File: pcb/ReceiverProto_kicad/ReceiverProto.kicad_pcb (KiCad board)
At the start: 4 copper layers, 75 x 50 mm, 65 parts, among them J1 Conn_01x09, J2 Conn_01x03, J3 Conn_01x04, J4 Conn_01x06, U11 ADM8660ARZ-REEL, U12 ADP7182AUJZ-1.8-R7, U13 ADA4807-1, U14 ADA4807-1, U15 ADA4807-1, U16 ADA4807-1, U4 AD7387BCPZ-RL7, U5 TLV9001IDCK, U6 TLV9001IDCK, U7 TPS79301DBVR

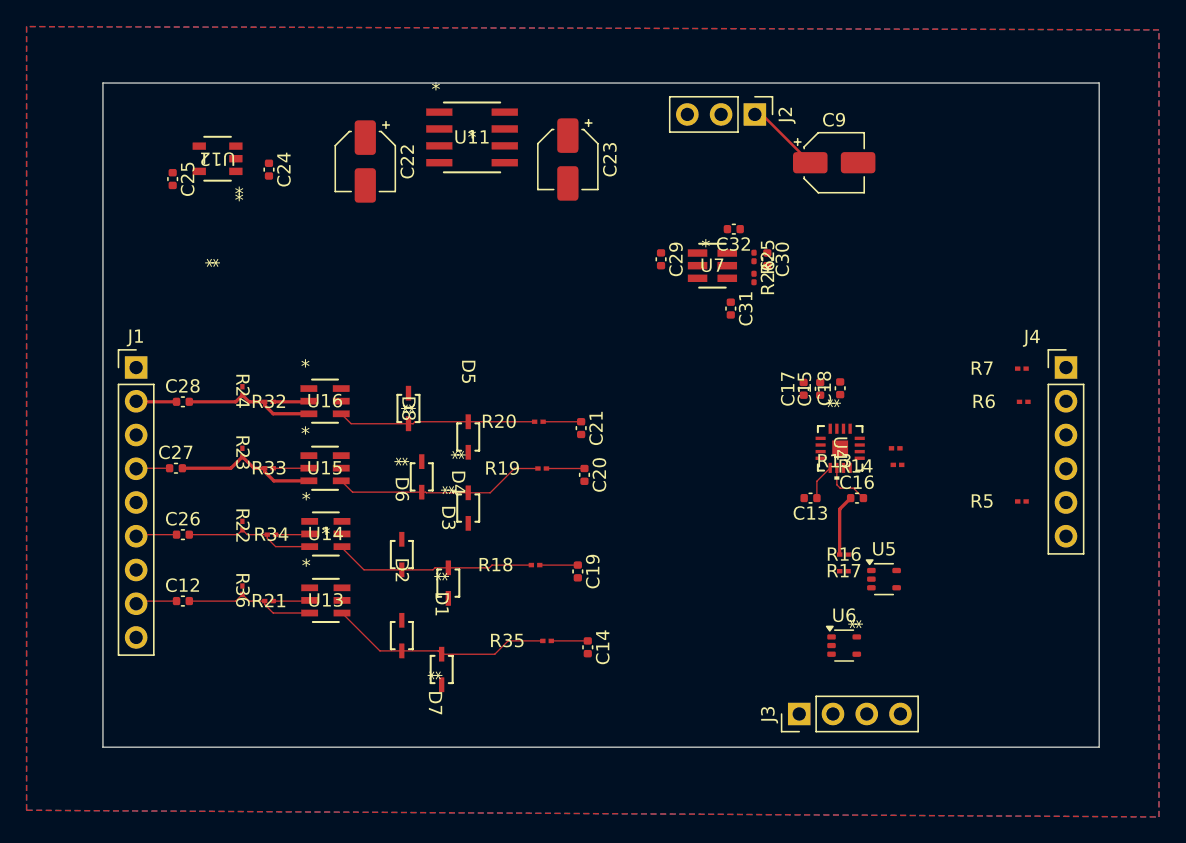
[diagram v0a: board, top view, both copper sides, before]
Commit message: completed majority of routing, a good portion of remaining routing will likely need to be on different layers.
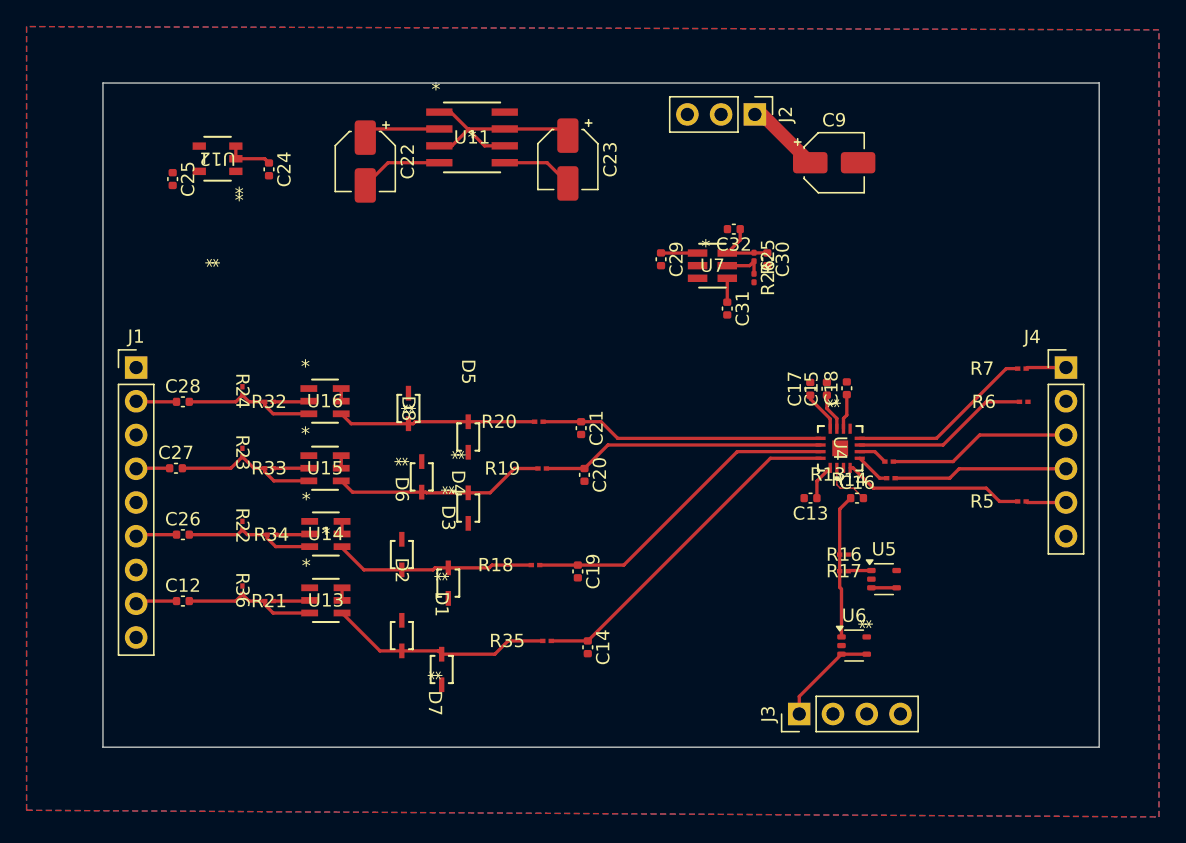
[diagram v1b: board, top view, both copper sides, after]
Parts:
- moved R13 1.12 mm to (164.7, 118.0)
- moved R14 1.12 mm to (164.8, 119.2)
- moved U6 0.75 mm to (162.1, 131.8)
- moved C15 0.50 mm to (160.0, 112.5)
- moved C17 0.50 mm to (158.8, 112.5)
- moved C18 0.50 mm to (161.5, 112.5)
- moved C31 0.26 mm to (152.5, 106.5)
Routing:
- net /adc/ADC_AINA0: track 2.75 -> 26.0 mm
- net /adc/ADC_AINA1: track 2.87 -> 24.7 mm
- net /adc/ADC_AINB1: track 2.87 -> 21.4 mm
- net /adc/ADC_AINB0: track 2.87 -> 21.4 mm
- net 0: track 3.69 -> 20.1 mm
- net ADC_SCLK: track 0.00 -> 14.1 mm
- net ADC_SDOB: track 0.00 -> 13.8 mm
- net ADC_CS: track 0.00 -> 13.7 mm
- net ADC_SDI: track 0.00 -> 13.4 mm
- net ADC_SDOA: track 0.00 -> 13.2 mm
- net +3V3: track 0.00 -> 11.1 mm
- net -5V: track 0.00 -> 8.97 mm
- net VREF: track 0.00 -> 7.72 mm
- net +5V: track 5.68 -> 12.2 mm
- net Net-(U11-CAP): track 0.00 -> 6.28 mm
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
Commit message: finished board layout, lots of warnings, ideally we remove designators and values that aren't on silkscreen.: clear
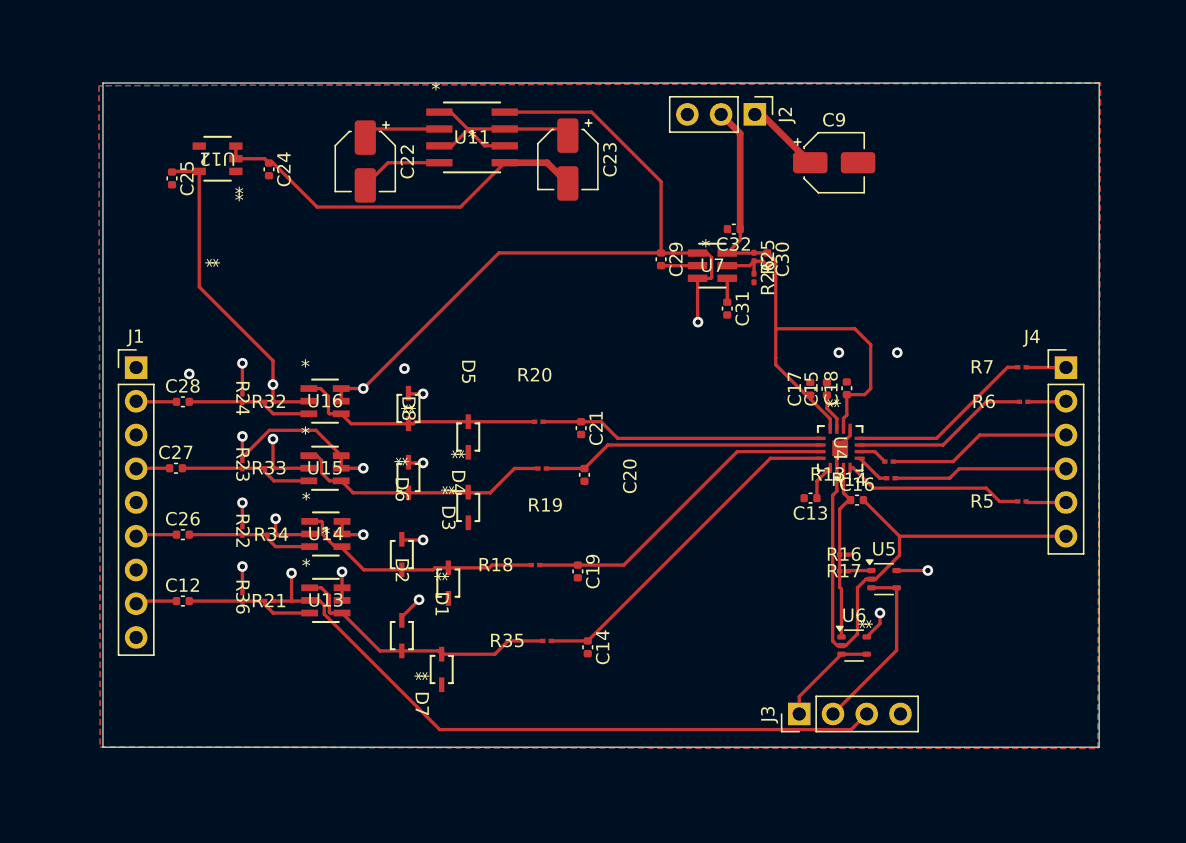
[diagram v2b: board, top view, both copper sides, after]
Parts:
- moved D7 1.00 mm to (128.5, 119.2)
- moved R23 0.90 mm to (116.0, 118.2)
- moved R24 0.53 mm to (116.0, 113.2)
- moved R36 0.50 mm to (116.0, 128.2)
- moved R22 0.40 mm to (116.0, 123.2)
- moved C16 0.15 mm to (162.3, 120.9)
- moved R7 0.10 mm to (174.7, 110.9)
- moved C25 0.07 mm to (110.7, 96.7)
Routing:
- net +5V: track 12.2 -> 155.0 mm, vias 0 -> 11
- net -2V5: track 10.7 -> 93.4 mm, vias 0 -> 4
- net 0: track 20.1 -> 86.2 mm, vias 0 -> 4
- net +3V3: track 11.1 -> 45.5 mm
- net /adc/Vref: track 0.00 -> 21.6 mm, vias 0 -> 4
- net -5V: track 8.97 -> 29.5 mm
- net VREF_DIV2: track 1.90 -> 13.4 mm
- net Net-(D5-K): track 14.9 -> 18.9 mm
- net Net-(D1-K): track 16.8 -> 20.8 mm
- net Net-(D4-K): track 16.0 -> 19.7 mm
- net Net-(D3-K): track 15.2 -> 18.8 mm
- net Net-(J4-Pin_2): track 0.00 -> 2.88 mm
- net /adc/ADC_REFIO: track 10.8 -> 13.5 mm
- net Net-(U7-FB): track 3.10 -> 4.24 mm
- net ADC_B0: track 3.30 -> 2.48 mm
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
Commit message: 0 net is now gnd; changed power routing to inner copper layer 2; added labels; few tweaks to routing and track width; arranged component identifiers
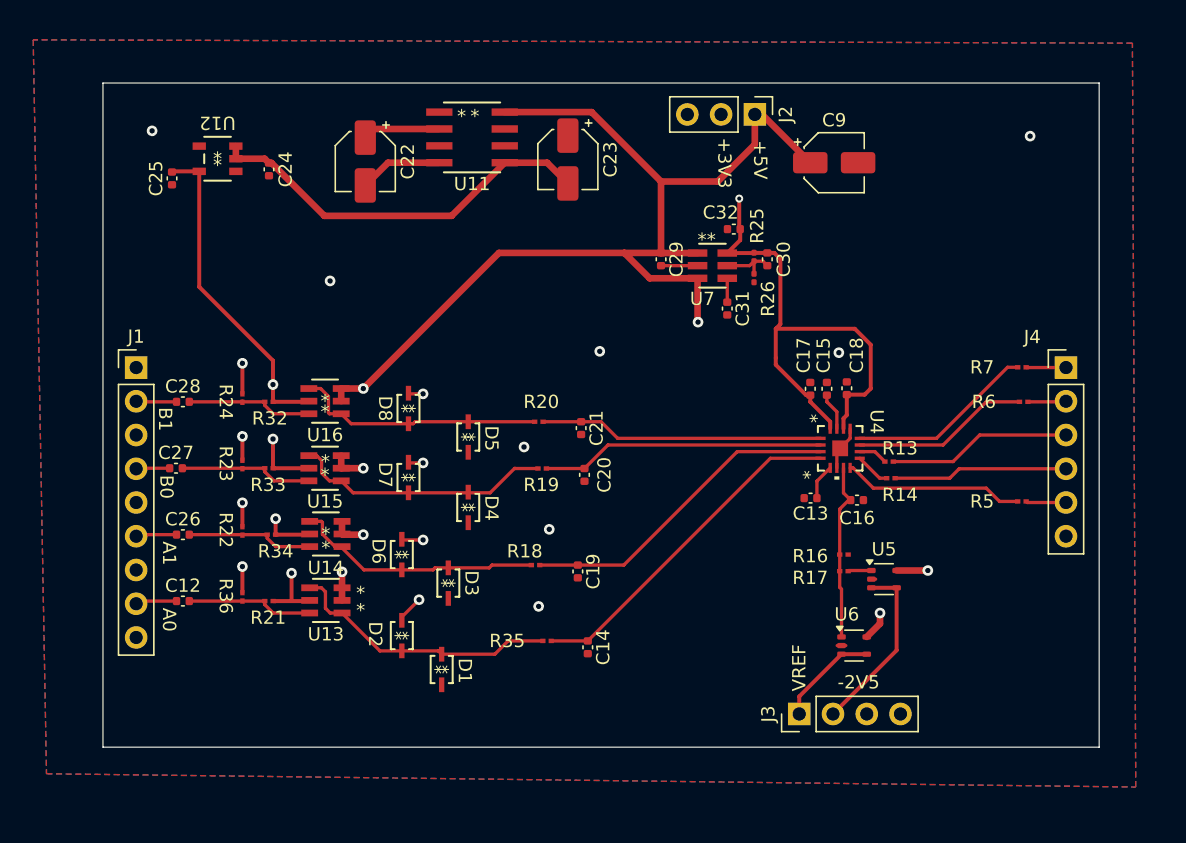
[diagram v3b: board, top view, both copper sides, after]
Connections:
- net 0 renamed GND
- D2 pad 1: /adc/Vref -> VREF
- D6 pad 1: /adc/Vref -> VREF
- D7 pad 1: /adc/Vref -> VREF
- D8 pad 1: /adc/Vref -> VREF
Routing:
- net GND: track 86.2 -> 7.79 mm, vias 4 -> 8
- net VREF: track 7.72 -> 61.9 mm, vias 0 -> 4
- net +5V: track 155.0 -> 194.2 mm
- net /adc/Vref: track 21.6 -> 0.00 mm, vias 4 -> 0
- net -2V5: track 93.4 -> 101.4 mm
- net +3V3: track 45.5 -> 46.0 mm, vias 0 -> 1
- net -5V: track 29.5 -> 30.0 mm
- added copper zone on In2.Cu, net GND
- removed copper zone on In2.Cu, net +3V3
- removed copper zone on In2.Cu, net +5V
- removed copper zone on In2.Cu, net -2V5
- removed copper zone on In2.Cu, net -5V
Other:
- board text added: "+3V3"
- board text added: "+5V"
- board text added: "-2V5"
- board text added: "A0"
- board text added: "A1"
- board text added: "B0"
- board text added: "B1"
- board text added: "VREF"
